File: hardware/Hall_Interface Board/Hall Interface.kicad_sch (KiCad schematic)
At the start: 10 parts, among them J8 LZSR 80-P

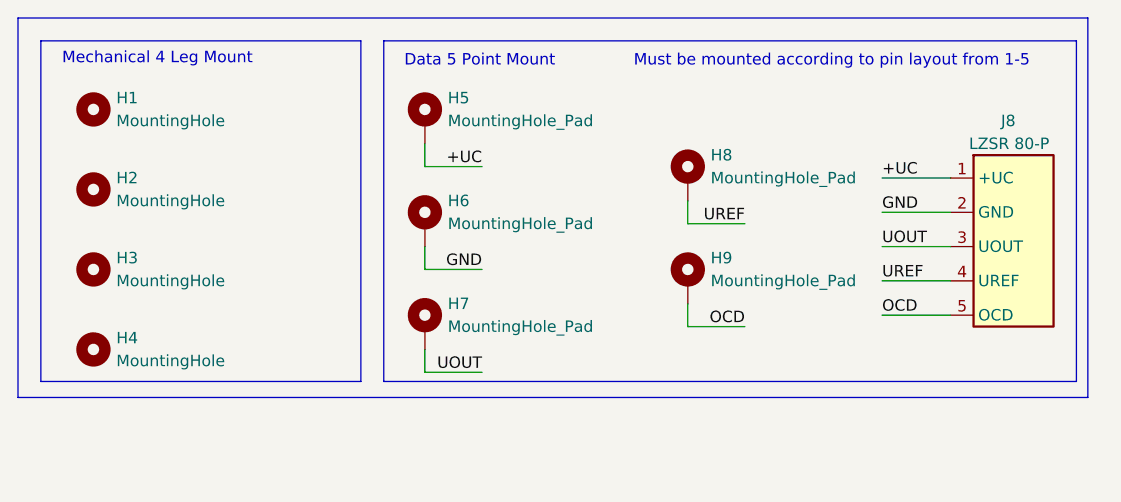
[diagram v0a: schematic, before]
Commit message: hall sensor footprint
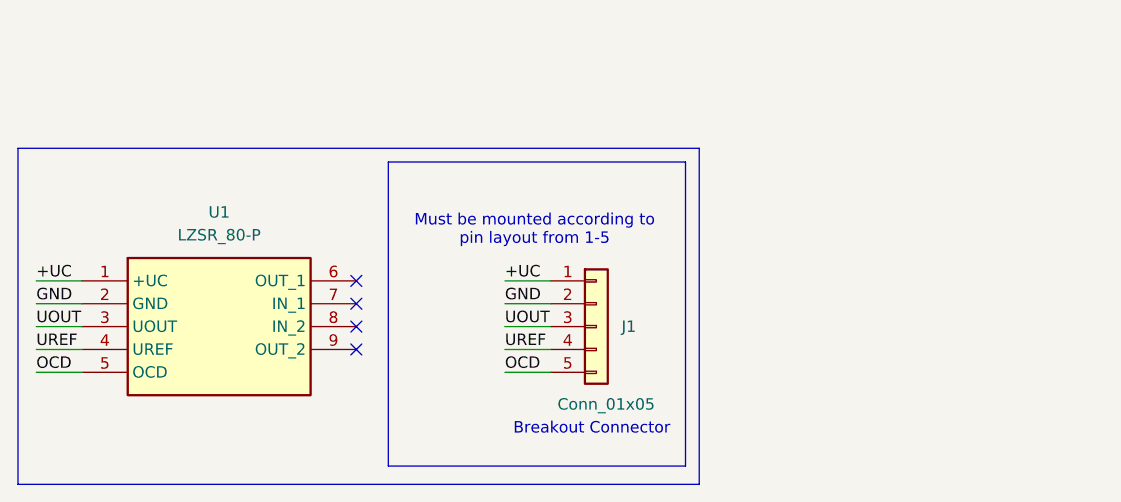
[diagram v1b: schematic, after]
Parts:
- removed H1, H2, H3, H4: MountingHole, MountingHole:MountingHole_2.0mm, symbol Mechanical:MountingHole
- removed H5, H6, H7, H8, H9: MountingHole_Pad, MountingHole:MountingHole_1.0mm, symbol Mechanical:MountingHole_Pad
- removed J8: LZSR 80-P, LHRS_Connectors:Molex_Nano-Fit_105309-xx05_1x05_P2.50mm_Vertical, symbol lhrs_connectors:CAN_NANO_01x05
- added J1: Conn_01x05, LHRS_Connectors:Molex_Nano-Fit_105309-xx05_1x05_P2.50mm_Vertical, symbol Connector_Generic:Conn_01x05
- added U1: LZSR_80-P, lzsr80p:LZSR80P, symbol LZSR_80-P:LZSR_80-P
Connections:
- net +UC: now also J1.1 (Pin_1), U1.1 (+UC)
- net GND: now also J1.2 (Pin_2), U1.2 (GND)
- net OCD: now also J1.5 (Pin_5), U1.5 (OCD)
- net UOUT: now also J1.3 (Pin_3), U1.3 (UOUT)
- net UREF: now also J1.4 (Pin_4), U1.4 (UREF)
- no-connect marks 0 -> 4
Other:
- note added: "Breakout Connector"
- note removed: "Data 5 Point Mount"
- note removed: "Mechanical 4 Leg Mount"
